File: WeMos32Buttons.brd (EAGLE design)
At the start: 86.4 x 27.9 mm, 9 parts, among them J1 Digital_8_13, J3 Digital_8_13

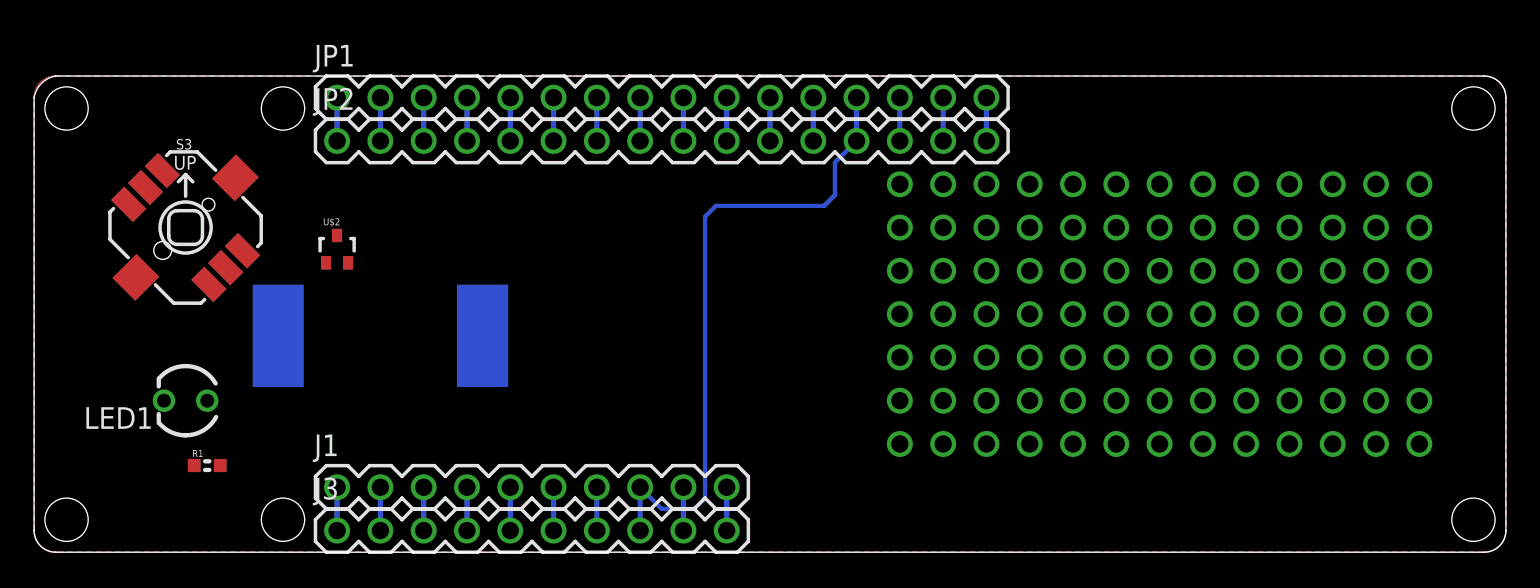
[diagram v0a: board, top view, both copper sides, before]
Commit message: Added pull-ups on all inputs, restructured to fit fake WeMos board
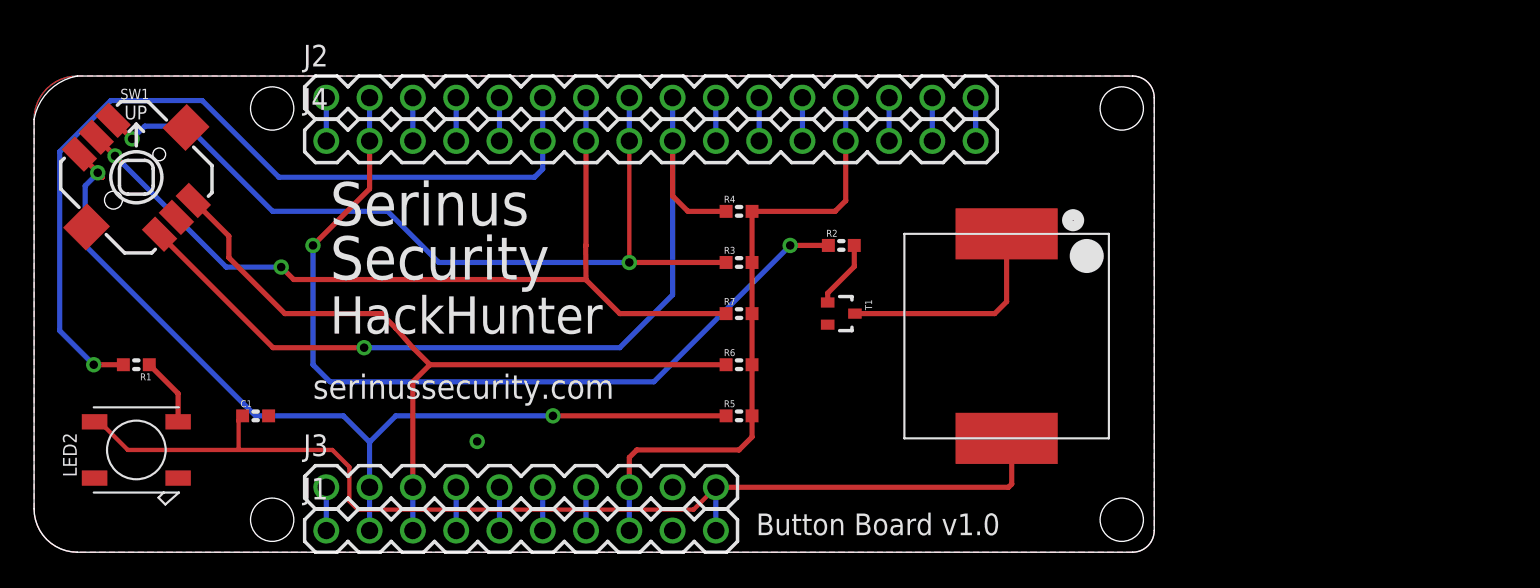
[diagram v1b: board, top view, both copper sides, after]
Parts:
- removed JP1, JP2: M16PTH, freetronics-jon:1X16
- removed LED1: (no value), freetronics-jon:LED3MM
- removed S3: (no value), SparkFun-Switches:JOYSTICK_MINI
- removed SG1: BUZZERSMD12X12, freetronics-master-v1.1:BUZZER-12X12-SMT
- removed U$2: MOSFET-NSOT-323, freetronics-jon:SOT32-3
- added C1: 100nF, freetronics-jon:0603
- added J2, J4: M16PTH, freetronics-jon:1X16
- added LED2: WS2812B5050, freetronics-jon:WS2812B
- added PIEZO1: BUZZERSMD12X12, freetronics-master-v1.1:BUZZER-12X12-SMT
- added R2: 470R, freetronics-jon:0603
- added R3, R4, R5, R6, R7: 22K, freetronics-jon:0603
- added SW1: (no value), SparkFun-Switches:JOYSTICK_MINI
- added T1: MOSFET-NSOT-323, freetronics-jon:SOT32-3
- moved R1 7.24 mm to (6.00, 11.0), turned to 180 degrees
- moved J1 2.62 mm to (17.1, 1.27)
- moved J3 2.62 mm to (17.1, 3.81)
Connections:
- removed net N$247: R1.2
- new net N$8: PIEZO1.1, T1.3
- new net N$9: R2.2, T1.1
- net 3.3V: now also J2.13, J4.13, R3.2, R4.2, R5.2, R6.2, R7.2; no longer JP1.13, JP2.13
- net 5V: now also C1.1, LED2.1-VDD, PIEZO1.2
- net GND: now also C1.2, J2.14, J2.15, J4.14, J4.15, LED2.3-GND, SW1.GND, T1.2; no longer JP1.14, JP1.15, JP2.14, JP2.15, LED1.K, S3.GND
- net GPIO0: now also J2.5, J4.5; no longer JP1.5, JP2.5
- net GPIO12: now also J2.8, J4.8, R3.1, SW1.A; no longer JP1.8, JP2.8
- net GPIO13: now also J2.9, J4.9, R4.1, SW1.D; no longer JP1.9, JP2.9
- net GPIO14: now also J2.7, J4.7, R7.1, SW1.CTR; no longer JP1.7, JP2.7
- net GPIO15: now also J2.10, J4.10; no longer JP1.10, JP2.10
- net GPIO16: now also J2.2, J4.2, R2.1; no longer JP1.2, JP2.2
- net GPIO2: now also J2.6, J4.6, R1.2; no longer JP1.6, JP2.6
- net GPIO25: now also R5.1, SW1.C
- net GPIO26: now also R6.1, SW1.B
- net GPIO4: now also J2.4, J4.4; no longer JP1.4, JP2.4
- net GPIO5: now also J2.3, J4.3; no longer JP1.3, JP2.3
- net N$118: now also J2.16, J4.16; no longer JP1.16, JP2.16
- net N$246: now also LED2.4-DIN; no longer LED1.A
- net RX: now also J2.11, J4.11; no longer JP1.11, JP2.11
- net SVN: now also J2.1, J4.1; no longer JP1.1, JP2.1
- net TX: now also J2.12, J4.12; no longer JP1.12, JP2.12
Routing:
- net 5V: track 2.54 -> 65.8 mm
- net GPIO25: track 2.54 -> 55.1 mm, vias 0 -> 2
- net GPIO14: track 2.54 -> 52.7 mm, vias 0 -> 2
- net GPIO13: track 2.54 -> 52.5 mm, vias 0 -> 1
- net GPIO16: track 2.54 -> 51.0 mm, vias 0 -> 2
- net GPIO2: track 2.54 -> 50.9 mm, vias 0 -> 1
- net GPIO12: track 2.54 -> 49.7 mm, vias 0 -> 2
- net GPIO26: track 2.54 -> 46.2 mm
- net N$8: track 0.00 -> 13.2 mm
- net N$246: track 0.00 -> 4.05 mm
- net N$9: track 0.00 -> 4.00 mm
- net GND: track 7.62 -> 5.08 mm, vias 0 -> 1
- net 3.3V: track 38.0 -> 37.0 mm
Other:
- board size 86.4 x 27.9 mm -> 65.7 x 27.9 mm
- board text added: "(C)2018 Serinus Security Pty Ltd All Rights Reserved"
- board text added: "Button Board v1.0"
- board text added: "HackHunter"
- board text added: "Serinus Security"
- board text added: "serinussecurity.com"

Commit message: Removed branding
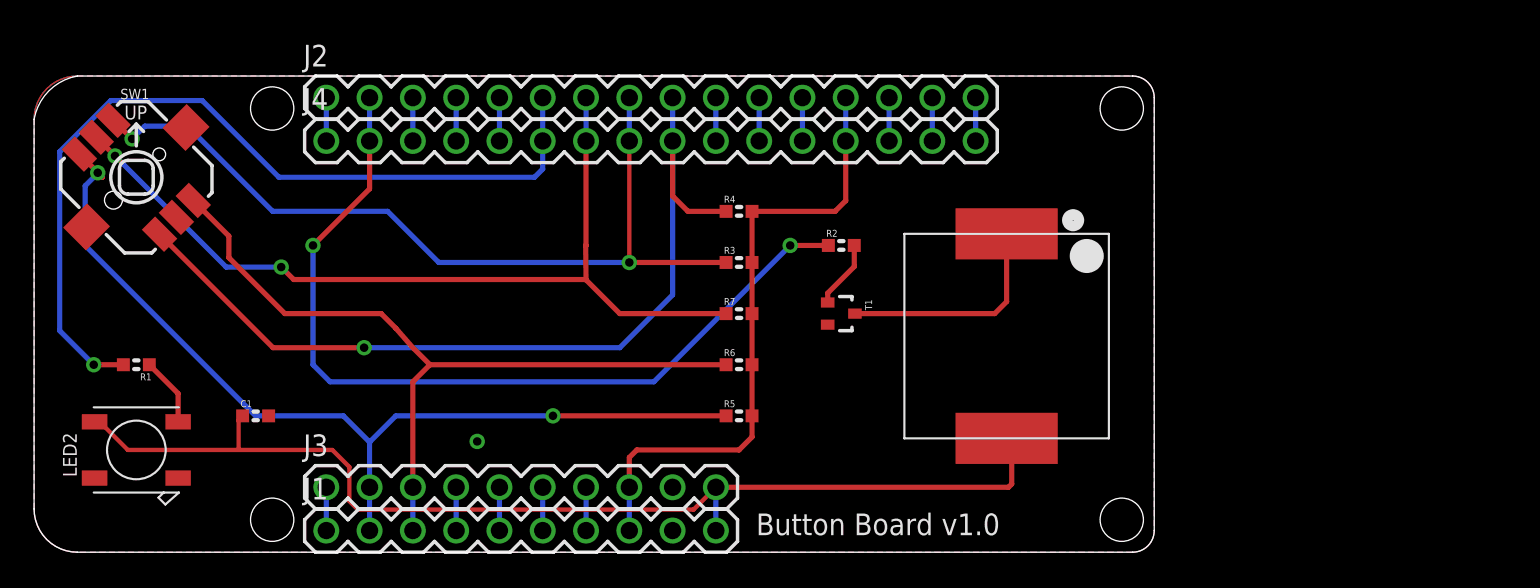
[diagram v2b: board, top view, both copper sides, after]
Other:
- board text added: "(C)2018 Freetronics Pty Ltd All Rights Reserved"
- board text removed: "(C)2018 Serinus Security Pty Ltd All Rights Reserved"
- board text removed: "HackHunter"
- board text removed: "Serinus Security"
- board text removed: "serinussecurity.com"
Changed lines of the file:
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@@
 <?xml version="1.0" encoding="utf-8"?>
 <!DOCTYPE eagle SYSTEM "eagle.dtd">
-<eagle version="8.7.0">
+<eagle version="9.3.0">
 <drawing>
 <settings>
@@
 <hole x="63.82" y="1.905" drill="2.54"/>
 <hole x="63.82" y="26.035" drill="2.54"/>
-<text x="17.365" y="16" size="2.54" layer="21" font="vector" ratio="16" distance="25">Serinus
-Security</text>
-<text x="16.365" y="9" size="1.4224" layer="21" font="vector" ratio="16" distance="25">serinussecurity.com</text>
-<text x="17.365" y="12.827" size="2.1844" layer="21" font="vector" ratio="16" distance="25">HackHunter</text>
-<text x="63.145" y="4.11" size="1.27" layer="22" font="vector" ratio="16" rot="MR0">(C)2018 Serinus Security Pty Ltd
+<text x="63.145" y="4.11" size="1.27" layer="22" font="vector" ratio="16" rot="MR0">(C)2018 Freetronics Pty Ltd
 All Rights Reserved</text>
 <text x="42.365" y="1" size="1.27" layer="21" font="vector" ratio="16">Button Board v1.0</text>
@@
 <param name="checkStop" value="0"/>
 <param name="checkValues" value="0"/>
+<param name="checkNames" value="1"/>
+<param name="checkWireStubs" value="1"/>
+<param name="checkPolygonWidth" value="0"/>
 <param name="useDiameter" value="13"/>
 <param name="maxErrors" value="50"/>
@@
 </autorouter>
 <elements>
-<element name="J1" library="freetronics-original" package="1X10" value="Digital_8_13" x="17.145" y="1.27"/>
-<element name="J2" library="freetronics-jon" package="1X16" value="M16PTH" x="17.145" y="26.67"/>
-<element name="J4" library="freetronics-jon" package="1X16" value="M16PTH" x="17.145" y="24.13"/>
-<element name="J3" library="freetronics-original" package="1X10" value="Digital_8_13" x="17.145" y="3.81"/>
-<element name="SW1" library="SparkFun-Switches" package="JOYSTICK_MINI" value="" x="6" y="22" rot="R315">
+<element name="J1" library="freetronics-original" package="1X10" value="Digital_8_13" x="17.145" y="1.27" smashed="yes">
+<attribute name="NAME" x="15.7988" y="3.0988" size="1.27" layer="25" ratio="10"/>
+<attribute name="VALUE" x="15.875" y="-1.905" size="1.27" layer="27"/>
+</element>
+<element name="J2" library="freetronics-jon" package="1X16" value="M16PTH" x="17.145" y="26.67" smashed="yes">
+<attribute name="NAME" x="15.7988" y="28.4988" size="1.27" layer="25" ratio="10"/>
+<attribute name="VALUE" x="15.875" y="23.495" size="1.27" layer="27"/>
+</element>
+<element name="J4" library="freetronics-jon" package="1X16" value="M16PTH" x="17.145" y="24.13" smashed="yes">
+<attribute name="NAME" x="15.7988" y="25.9588" size="1.27" layer="25" ratio="10"/>
+<attribute name="VALUE" x="15.875" y="20.955" size="1.27" layer="27"/>
+</element>
+<element name="J3" library="freetronics-original" package="1X10" value="Digital_8_13" x="17.145" y="3.81" smashed="yes">
+<attribute name="NAME" x="15.7988" y="5.6388" size="1.27" layer="25" ratio="10"/>
+<attribute name="VALUE" x="15.875" y="0.635" size="1.27" layer="27"/>
+</element>
+<element name="SW1" library="SparkFun-Switches" package="JOYSTICK_MINI" value="" x="6" y="22" smashed="yes" rot="R315">
+<attribute name="NAME" x="5.910196875" y="26.579928125" size="0.6096" layer="25" font="vector" ratio="20" align="bottom-center"/>
 <attribute name="PROD_ID" value="SWCH-09905" x="6" y="22" size="1.778" layer="27" rot="R315" display="off"/>
 <attribute name="SF_SKU" value="COM-10063" x="6" y="22" size="1.778" layer="27" rot="R315" display="off"/>
-</element>
-<element name="R1" library="freetronics-jon" package="0603" value="470R" x="6" y="11" rot="R180"/>
-<element name="PIEZO1" library="freetronics-master-v1.1" package="BUZZER-12X12-SMT" value="BUZZERSMD12X12" x="57.065" y="12.68" rot="R270"/>
-<element name="T1" library="freetronics-jon" package="SOT32-3" value="MOSFET-NSOT-323" x="47.365" y="14" rot="R270"/>
-<element name="R2" library="freetronics-jon" package="0603" value="470R" x="47.365" y="18"/>
-<element name="R3" library="freetronics-jon" package="0603" value="22K" x="41.365" y="17"/>
-<element name="R4" library="freetronics-jon" package="0603" value="22K" x="41.365" y="20"/>
-<element name="R5" library="freetronics-jon" package="0603" value="22K" x="41.365" y="8"/>
-<element name="R6" library="freetronics-jon" package="0603" value="22K" x="41.365" y="11"/>
-<element name="R7" library="freetronics-jon" package="0603" value="22K" x="41.365" y="14"/>
-<element name="LED2" library="freetronics-jon" package="WS2812B" value="WS2812B5050" x="6" y="6" rot="R180"/>
-<element name="C1" library="freetronics-jon" package="0603" value="100nF" x="13" y="8"/>
+<attribute name="VALUE" x="6.179603125" y="17.509871875" size="0.6096" layer="27" font="vector" ratio="20" align="top-center"/>
+</element>
+<element name="R1" library="freetronics-jon" package="0603" value="470R" x="6" y="11" smashed="yes" rot="R180">
+<attribute name="NAME" x="6.889" y="10.492" size="0.4064" layer="25" font="vector" rot="R180"/>
+<attribute name="VALUE" x="7.016" y="11.9652" size="0.4064" layer="27" font="vector" rot="R180"/>
+</element>
+<element name="PIEZO1" library="freetronics-master-v1.1" package="BUZZER-12X12-SMT" value="BUZZERSMD12X12" x="57.065" y="12.68" smashed="yes" rot="R270"/>
+<element name="T1" library="freetronics-jon" package="SOT32-3" value="MOSFET-NSOT-323" x="47.365" y="14" smashed="yes" rot="R270">
+<attribute name="NAME" x="48.765" y="14.8255" size="0.4064" layer="25" rot="R270"/>
+<attribute name="VALUE" x="47.1745" y="14.8" size="0.3048" layer="27" rot="R270"/>
+</element>
+<element name="R2" library="freetronics-jon" package="0603" value="470R" x="47.365" y="18" smashed="yes">
+<attribute name="NAME" x="46.476" y="18.508" size="0.4064" layer="25" font="vector"/>
+<attribute name="VALUE" x="46.349" y="17.0348" size="0.4064" layer="27" font="vector"/>
+</element>
+<element name="R3" library="freetronics-jon" package="0603" value="22K" x="41.365" y="17" smashed="yes">
+<attribute name="NAME" x="40.476" y="17.508" size="0.4064" layer="25" font="vector"/>
+<attribute name="VALUE" x="40.349" y="16.0348" size="0.4064" layer="27" font="vector"/>
+</element>
+<element name="R4" library="freetronics-jon" package="0603" value="22K" x="41.365" y="20" smashed="yes">
+<attribute name="NAME" x="40.476" y="20.508" size="0.4064" layer="25" font="vector"/>
+<attribute name="VALUE" x="40.349" y="19.0348" size="0.4064" layer="27" font="vector"/>
+</element>
+<element name="R5" library="freetronics-jon" package="0603" value="22K" x="41.365" y="8" smashed="yes">
+<attribute name="NAME" x="40.476" y="8.508" size="0.4064" layer="25" font="vector"/>
+<attribute name="VALUE" x="40.349" y="7.0348" size="0.4064" layer="27" font="vector"/>
+</element>
+<element name="R6" library="freetronics-jon" package="0603" value="22K" x="41.365" y="11" smashed="yes">
+<attribute name="NAME" x="40.476" y="11.508" size="0.4064" layer="25" font="vector"/>
+<attribute name="VALUE" x="40.349" y="10.0348" size="0.4064" layer="27" font="vector"/>
+</element>
+<element name="R7" library="freetronics-jon" package="0603" value="22K" x="41.365" y="14" smashed="yes">
+<attribute name="NAME" x="40.476" y="14.508" size="0.4064" layer="25" font="vector"/>
+<attribute name="VALUE" x="40.349" y="13.0348" size="0.4064" layer="27" font="vector"/>
+</element>
+<element name="LED2" library="freetronics-jon" package="WS2812B" value="WS2812B5050" x="6" y="6" smashed="yes" rot="R180">
+<attribute name="NAME" x="2.5075" y="4.4125" size="0.8128" layer="25" ratio="10" rot="R90"/>
+</element>
+<element name="C1" library="freetronics-jon" package="0603" value="100nF" x="13" y="8" smashed="yes">
+<attribute name="NAME" x="12.111" y="8.508" size="0.4064" layer="25" font="vector"/>
+<attribute name="VALUE" x="11.984" y="7.0348" size="0.4064" layer="27" font="vector"/>
+</element>
 </elements>
 <signals>
@@
 </signal>
 </signals>
+<mfgpreviewcolors>
+<mfgpreviewcolor name="soldermaskcolor" color="0xC8008000"/>
+<mfgpreviewcolor name="silkscreencolor" color="0xFFFEFEFE"/>
+<mfgpreviewcolor name="backgroundcolor" color="0xFF282828"/>
+<mfgpreviewcolor name="coppercolor" color="0xFFFFBF00"/>
+<mfgpreviewcolor name="substratecolor" color="0xFF786E46"/>
+</mfgpreviewcolors>
 <errors>
 </errors>
